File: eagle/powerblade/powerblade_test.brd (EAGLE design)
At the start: 123 x 88 mm, 78 parts, among them J1 JTAG_14PIN_IDC-NL, J21 AC_INFILM, Q1 2N7002, U1 TPS62122, U2 AD524, U3 MSP430FR5738, U4 LTC5800, U5 MAX9910, U6 MAX9910

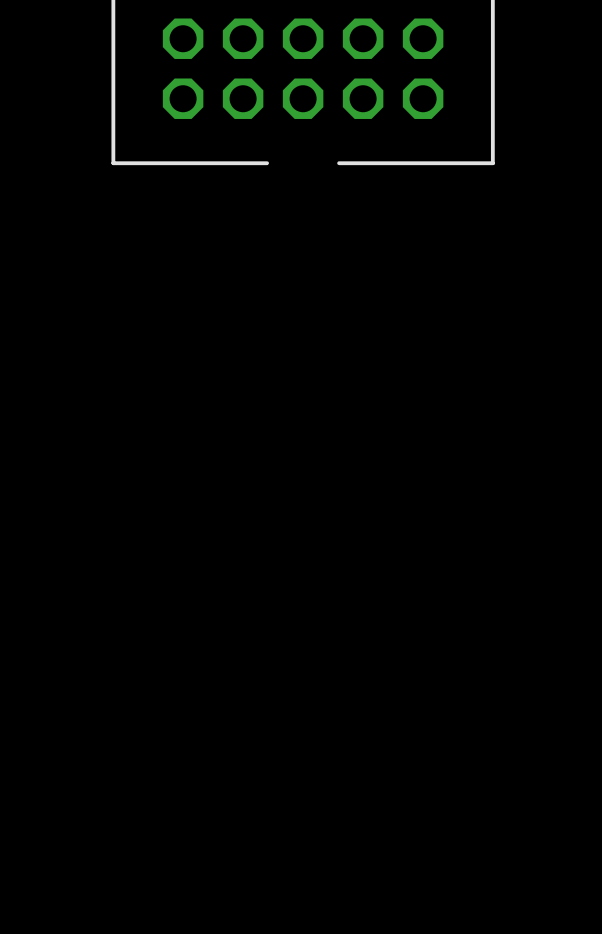
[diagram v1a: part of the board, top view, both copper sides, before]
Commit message: added crystals to ltc5800 sch in powerblade test
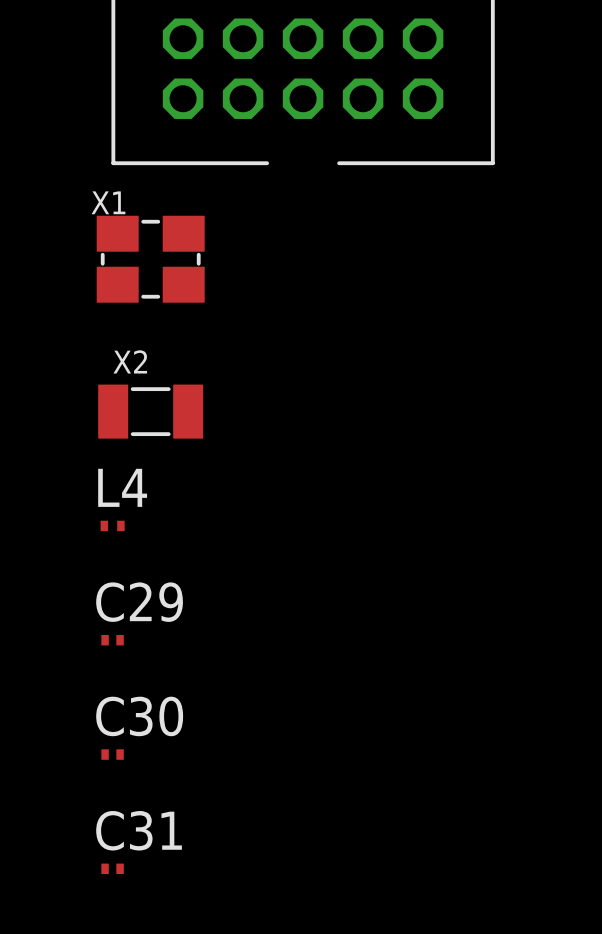
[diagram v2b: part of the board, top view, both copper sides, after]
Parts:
- added C29, C30: 1pF, rcl:C0201
- added C31: 100pF, rcl:C0201
- added L4: 3.3nH, rcl:L0201
- added X1: ABM8G, powerfilm:ABM8G
- added X2: ABS07, powerfilm:ABS07
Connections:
- new net N$42: U4.P29, X1.P1
- new net N$43: U4.P28, X1.P3
- new net N$44: U4.P20, X2.P2
- new net N$45: U4.P19, X2.P1
- new net N$46: C29.1, L4.2, U4.P14
- new net N$47: C30.1, C31.1, L4.1
- net GND: now also C29.2, C30.2, X1.P2, X1.P4
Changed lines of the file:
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@@
 <?xml version="1.0" encoding="utf-8"?>
 <!DOCTYPE eagle SYSTEM "eagle.dtd">
-<eagle version="6.3">
+<eagle version="6.5.0">
 <drawing>
 <settings>
@@
 <attribute name="DIGIKEY" value="WM18560-ND" x="-35.56" y="-135.89" size="1.778" layer="27" display="off"/>
 </element>
+<element name="X1" library="powerfilm" package="ABM8G" value="ABM8G" x="-40.64" y="-142.24">
+<attribute name="DIGIKEY" value="535-10293-1-ND" x="-40.64" y="-142.24" size="1.778" layer="27" display="off"/>
+</element>
+<element name="X2" library="powerfilm" package="ABS07" value="ABS07" x="-40.64" y="-147.32">
+<attribute name="DIGIKEY" value="535-12058-1-ND" x="-40.64" y="-147.32" size="1.778" layer="27" display="off"/>
+</element>
+<element name="L4" library="rcl" package="L0201" value="3.3nH" x="-41.91" y="-151.13"/>
+<element name="C29" library="rcl" package="C0201" value="1pF" x="-41.91" y="-154.94"/>
+<element name="C30" library="rcl" package="C0201" value="1pF" x="-41.91" y="-158.75"/>
+<element name="C31" library="rcl" package="C0201" value="100pF" x="-41.91" y="-162.56"/>
 </elements>
 <signals>
@@
 <vertex x="0" y="88.9"/>
 </polygon>
+<contactref element="X1" pad="P2"/>
+<contactref element="X1" pad="P4"/>
+<contactref element="C30" pad="2"/>
+<contactref element="C29" pad="2"/>
+<wire x1="-41.66" y1="-154.94" x2="-41.66" y2="-158.75" width="0" layer="19" extent="1-1"/>
+<wire x1="-39.54" y1="-143.09" x2="-41.66" y2="-154.94" width="0" layer="19" extent="1-1"/>
+<wire x1="-41.74" y1="-141.39" x2="-39.54" y2="-143.09" width="0" layer="19" extent="1-1"/>
+<wire x1="-33.56" y1="-134.89" x2="-39.54" y2="-143.09" width="0" layer="19" extent="1-1"/>
 <wire x1="-33.97" y1="-128.27" x2="-33.56" y2="-134.89" width="0" layer="19" extent="1-1"/>
 <wire x1="-37.78" y1="-128.27" x2="-33.97" y2="-128.27" width="0" layer="19" extent="1-1"/>
@@
 <wire x1="-38.1" y1="-25.4" x2="-41.26" y2="-66.04" width="0" layer="19" extent="1-1"/>
 <wire x1="-29.36875" y1="-23.23375" x2="-38.1" y2="-25.4" width="0" layer="19" extent="1-1"/>
+<wire x1="-27.375" y1="-23.61" x2="-29.36875" y2="-23.23375" width="0" layer="19" extent="1-1"/>
+<wire x1="-26.15" y1="-22.86" x2="-26.15" y2="-23.61" width="0" layer="19" extent="1-1"/>
+<wire x1="-25.4" y1="-22.86" x2="-25.4" y2="-23.61" width="0" layer="19" extent="1-1"/>
+<wire x1="-24.65" y1="-23.61" x2="-25.4" y2="-23.61" width="0" layer="19" extent="1-1"/>
+<wire x1="-26.15" y1="-22.11" x2="-26.15" y2="-22.86" width="0" layer="19" extent="1-1"/>
+<wire x1="-29.298" y1="-20.16125" x2="-27.375" y2="-21.61" width="0" layer="19" extent="1-1"/>
+<wire x1="-29.04" y1="-18.105" x2="-29.845" y2="-18.7325" width="0" layer="19" extent="1-1"/>
+<wire x1="-27.94" y1="-18.25625" x2="-29.04" y2="-18.105" width="0" layer="19" extent="1-1"/>
+<wire x1="-26.84" y1="-18.105" x2="-27.94" y2="-18.25625" width="0" layer="19" extent="1-1"/>
+<wire x1="-28.575" y1="-26.40875" x2="-27.375" y2="-23.61" width="0" layer="19" extent="1-1"/>
+<wire x1="-26.67" y1="-27.94" x2="-28.575" y2="-26.40875" width="0" layer="19" extent="1-1"/>
+<wire x1="-28.73375" y1="-13.59625" x2="-29.04" y2="-18.105" width="0" layer="19" extent="1-1"/>
+<wire x1="-27.305" y1="-13.59625" x2="-28.73375" y2="-13.59625" width="0" layer="19" extent="1-1"/>
+<wire x1="-27.305" y1="-12.3825" x2="-27.305" y2="-13.59625" width="0" layer="19" extent="1-1"/>
+<wire x1="-20.8788" y1="-14.76375" x2="-27.305" y2="-13.59625" width="0" layer="19" extent="1-1"/>
+<wire x1="-19.79625" y1="-13.9225" x2="-20.8788" y2="-14.76375" width="0" layer="19" extent="1-1"/>
+<wire x1="-17.78" y1="-18.25625" x2="-20.8788" y2="-14.76375" width="0" layer="19" extent="1-1"/>
+<wire x1="-18.25625" y1="-9.04875" x2="-19.79625" y2="-13.9225" width="0" layer="19" extent="1-1"/>
+<wire x1="-15.01625" y1="-9.271" x2="-18.25625" y2="-9.04875" width="0" layer="19" extent="1-1"/>
+<wire x1="-14.0462" y1="-9.486" x2="-15.01625" y2="-9.271" width="0" layer="19" extent="1-1"/>
+<wire x1="-12.85875" y1="-8.5748" x2="-14.0462" y2="-9.486" width="0" layer="19" extent="1-1"/>
+<wire x1="-11.58875" y1="-8.5748" x2="-12.85875" y2="-8.5748" width="0" layer="19" extent="1-1"/>
+<wire x1="-11.34975" y1="-8.80975" x2="-11.58875" y2="-8.5748" width="0" layer="19" extent="1-1"/>
+<wire x1="-6.8375" y1="-10.2085" x2="-9.38125" y2="-8.80975" width="0" layer="19" extent="1-1"/>
+<wire x1="-8.31125" y1="-12.7635" x2="-6.8375" y2="-10.2085" width="0" layer="19" extent="1-1"/>
+<wire x1="-11.43" y1="-20.955" x2="-17.78" y2="-18.25625" width="0" layer="19" extent="1-1"/>
 <wire x1="28.79" y1="6.35" x2="-6.8375" y2="-10.2085" width="0" layer="19" extent="1-1"/>
 </signal>
@@
 <contactref element="RI1" pad="1"/>
 </signal>
+<signal name="N$42">
+<contactref element="U4" pad="P29"/>
+<contactref element="X1" pad="P1"/>
+<wire x1="-37.35" y1="-30.25" x2="-41.74" y2="-143.09" width="0" layer="19" extent="1-1"/>
+</signal>
+<signal name="N$43">
+<contactref element="U4" pad="P28"/>
+<contactref element="X1" pad="P3"/>
+<wire x1="-37.85" y1="-30.25" x2="-39.54" y2="-141.39" width="0" layer="19" extent="1-1"/>
+</signal>
+<signal name="N$44">
+<contactref element="U4" pad="P20"/>
+<contactref element="X2" pad="P2"/>
+<wire x1="-41.85" y1="-30.25" x2="-39.39" y2="-147.32" width="0" layer="19" extent="1-1"/>
+</signal>
+<signal name="N$45">
+<contactref element="U4" pad="P19"/>
+<contactref element="X2" pad="P1"/>
+<wire x1="-42.35" y1="-30.25" x2="-41.89" y2="-147.32" width="0" layer="19" extent="1-1"/>
+</signal>
+<signal name="N$46">
+<contactref element="U4" pad="P14"/>
+<contactref element="L4" pad="2"/>
+<contactref element="C29" pad="1"/>
+<wire x1="-41.635" y1="-151.13" x2="-42.16" y2="-154.94" width="0" layer="19" extent="1-1"/>
+<wire x1="-42.95" y1="-27.65" x2="-41.635" y2="-151.13" width="0" layer="19" extent="1-1"/>
+</signal>
+<signal name="N$47">
+<contactref element="L4" pad="1"/>
+<contactref element="C31" pad="1"/>
+<contactref element="C30" pad="1"/>
+<wire x1="-42.16" y1="-158.75" x2="-42.16" y2="-162.56" width="0" layer="19" extent="1-1"/>
+<wire x1="-42.185" y1="-151.13" x2="-42.16" y2="-158.75" width="0" layer="19" extent="1-1"/>
+</signal>
 </signals>

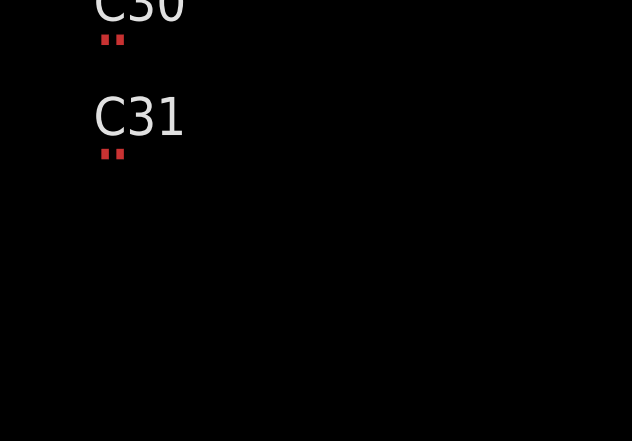
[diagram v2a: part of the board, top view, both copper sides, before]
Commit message: added antenna and programming header to ltc5800 schematic
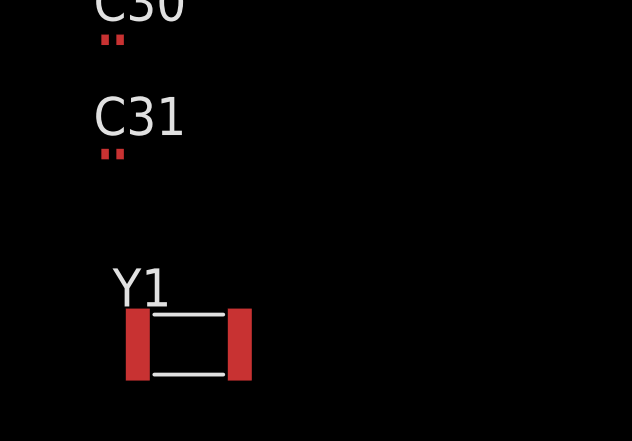
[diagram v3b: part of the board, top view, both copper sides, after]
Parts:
- added Y1: UREACH_XTEND, powerfilm:UREACH_XTEND
- C29: value 1pF -> 1.2pF
- C30: value 1pF -> NP
- C31: value 100pF -> 0ohm
- L4: value 3.3nH -> 7.5nH
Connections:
- new net FLASH_EN: SV1.2, U4.P55
- new net IPC_MISO: SV1.5, U4.P40
- new net IPC_MOSI: SV1.4, U4.P42
- new net IPC_SCK: SV1.3, U4.P44
- new net IPC_SS: SV1.1, U4.P45
- new net N$48: C31.2, Y1.P1
- new net UC_RX: SV1.10, U4.P38
- new net UC_TX: SV1.9, U4.P37
- net +3V3: now also SV1.7
- net NRST: now also SV1.6
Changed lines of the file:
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@@
 <?xml version="1.0" encoding="utf-8"?>
 <!DOCTYPE eagle SYSTEM "eagle.dtd">
-<eagle version="6.5.0">
+<eagle version="6.3">
 <drawing>
 <settings>
@@
 <attribute name="DIGIKEY" value="535-12058-1-ND" x="-40.64" y="-147.32" size="1.778" layer="27" display="off"/>
 </element>
-<element name="L4" library="rcl" package="L0201" value="3.3nH" x="-41.91" y="-151.13"/>
-<element name="C29" library="rcl" package="C0201" value="1pF" x="-41.91" y="-154.94"/>
-<element name="C30" library="rcl" package="C0201" value="1pF" x="-41.91" y="-158.75"/>
-<element name="C31" library="rcl" package="C0201" value="100pF" x="-41.91" y="-162.56"/>
+<element name="L4" library="rcl" package="L0201" value="7.5nH" x="-41.91" y="-151.13"/>
+<element name="C29" library="rcl" package="C0201" value="1.2pF" x="-41.91" y="-154.94"/>
+<element name="C30" library="rcl" package="C0201" value="NP" x="-41.91" y="-158.75"/>
+<element name="C31" library="rcl" package="C0201" value="0ohm" x="-41.91" y="-162.56"/>
+<element name="Y1" library="powerfilm" package="UREACH_XTEND" value="UREACH_XTEND" x="-39.37" y="-168.91">
+<attribute name="FRACTUS" value="FR05-S1-N-0-110" x="-39.37" y="-168.91" size="1.778" layer="27" display="off"/>
+</element>
 </elements>
 <signals>
@@
 <contactref element="R15" pad="1"/>
 <contactref element="L2" pad="1"/>
+<contactref element="SV1" pad="7"/>
+<wire x1="-32.07" y1="-127.62" x2="-33.56" y2="-136.89" width="0" layer="19" extent="1-1"/>
+<wire x1="-35.88" y1="-127.62" x2="-32.07" y2="-127.62" width="0" layer="19" extent="1-1"/>
+<wire x1="-36.21" y1="-123.19" x2="-35.88" y2="-127.62" width="0" layer="19" extent="1-1"/>
+<wire x1="-42.56" y1="-123.19" x2="-36.21" y2="-123.19" width="0" layer="19" extent="1-1"/>
 <wire x1="-41.06" y1="-118.11" x2="-42.56" y2="-123.19" width="0" layer="19" extent="1-1"/>
-<wire x1="-36.21" y1="-123.19" x2="-42.56" y2="-123.19" width="0" layer="19" extent="1-1"/>
-<wire x1="-35.88" y1="-127.62" x2="-36.21" y2="-123.19" width="0" layer="19" extent="1-1"/>
-<wire x1="-32.07" y1="-127.62" x2="-35.88" y2="-127.62" width="0" layer="19" extent="1-1"/>
 <wire x1="-31.33" y1="-102.87" x2="-41.06" y2="-118.11" width="0" layer="19" extent="1-1"/>
 <wire x1="-42.76" y1="-97.79" x2="-31.33" y2="-102.87" width="0" layer="19" extent="1-1"/>
 <wire x1="-22.70125" y1="-29.21" x2="-42.76" y2="-97.79" width="0" layer="19" extent="1-1"/>
+<wire x1="-29.04" y1="-17.455" x2="-29.04" y2="-16.805" width="0" layer="19" extent="1-1"/>
+<wire x1="-28.73375" y1="-15.29625" x2="-29.04" y2="-16.805" width="0" layer="19" extent="1-1"/>
 </signal>
 <signal name="RST">
@@
 <signal name="NRST">
 <contactref element="U4" pad="P22"/>
+<contactref element="SV1" pad="6"/>
+<wire x1="-40.85" y1="-30.25" x2="-35.56" y2="-134.89" width="0" layer="19" extent="1-1"/>
 </signal>
 <signal name="N$37">
@@
 <wire x1="-42.185" y1="-151.13" x2="-42.16" y2="-158.75" width="0" layer="19" extent="1-1"/>
 </signal>
+<signal name="N$48">
+<contactref element="C31" pad="2"/>
+<contactref element="Y1" pad="P1"/>
+<wire x1="-41.66" y1="-162.56" x2="-41.07" y2="-168.91" width="0" layer="19" extent="1-1"/>
+</signal>
+<signal name="IPC_SS">
+<contactref element="SV1" pad="1"/>
+<contactref element="U4" pad="P45"/>
+<wire x1="-33.25" y1="-25.65" x2="-39.56" y2="-136.89" width="0" layer="19" extent="1-1"/>
+</signal>
+<signal name="IPC_SCK">
+<contactref element="SV1" pad="3"/>
+<contactref element="U4" pad="P44"/>
+<wire x1="-33.25" y1="-26.15" x2="-37.56" y2="-136.89" width="0" layer="19" extent="1-1"/>
+</signal>
+<signal name="IPC_MISO">
+<contactref element="SV1" pad="5"/>
+<contactref element="U4" pad="P40"/>
+<wire x1="-33.25" y1="-28.15" x2="-35.56" y2="-136.89" width="0" layer="19" extent="1-1"/>
+</signal>
+<signal name="UC_TX">
+<contactref element="SV1" pad="9"/>
+<contactref element="U4" pad="P37"/>
+<wire x1="-33.25" y1="-29.65" x2="-31.56" y2="-136.89" width="0" layer="19" extent="1-1"/>
+</signal>
+<signal name="FLASH_EN">
+<contactref element="SV1" pad="2"/>
+<contactref element="U4" pad="P55"/>
+<wire x1="-33.85" y1="-20.55" x2="-39.56" y2="-134.89" width="0" layer="19" extent="1-1"/>
+</signal>
+<signal name="IPC_MOSI">
+<contactref element="SV1" pad="4"/>
+<contactref element="U4" pad="P42"/>
+<wire x1="-33.25" y1="-27.15" x2="-37.56" y2="-134.89" width="0" layer="19" extent="1-1"/>
+</signal>
+<signal name="UC_RX">
+<contactref element="SV1" pad="10"/>
+<contactref element="U4" pad="P38"/>
+<wire x1="-33.25" y1="-29.15" x2="-31.56" y2="-134.89" width="0" layer="19" extent="1-1"/>
+</signal>
 </signals>

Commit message: added tr1000 to powerblade test sch
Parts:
- added C32, C33, C34: NP, rcl:C0603
- added C35: 27pF, rcl:C0603
- added C36: 100pF, rcl:C0603
- added C37: 4.7uF, rcl:CPOL-0805
- added R22: 270k, rcl:R0603
- added R23, R24, R27: 0, rcl:R0603
- added R25, R33, R34: NP, rcl:R0603
- added R26, R29: 100k, rcl:R0603
- added R28: 330k, rcl:R0603
- added R30: 4.7k, rcl:R0603
- added R31, R32: 4.99k, rcl:R0603
- C2: value 0.1uF -> 15nF
- R12: value 660 -> NP
- U2: value AD524 -> TR1000; device powerfilm:SOT-23-8 -> powerfilm:SM-20H
- moved R12 243.2 mm to (-50.8, -256.5), turned to 0 degrees
- moved C2 197.6 mm to (-50.8, -210.8), turned to 0 degrees
- moved U2 147.5 mm to (-48.3, -163.8)
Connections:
- removed net SCL: U2.P4, U3.P17
- removed net SDA: U2.P5, U3.P16
- new net CNT0: R32.2, U2.P18, U3.P1
- new net CNT1: R31.2, U2.P17, U3.P2
- new net N$49: C34.1, R23.1, U2.P3
- new net N$50: R12.2, R22.2, U2.P15
- new net N$51: R28.2, U2.P14
- new net N$52: R29.2, U2.P9
- new net N$53: R30.2, U2.P8
- new net N$54: C2.2, C32.1, R27.2
- new net N$55: C2.1, U2.P6
- new net N$56: R24.2, R25.2, R26.1, U2.P11
- new net N$57: R24.1, U2.P13
- new net N$58: R25.1, U2.P12
- new net N$59: C33.1, U2.P4
- new net N$60: R33.1, U3.P13
- new net N$61: R34.1, U3.P14
- new net RXDATA: R34.2, U2.P7, U3.P4
- new net TXMOD: R30.1, R33.2, U3.P3
- net +3V3: now also C35.1, C36.1, C37.+, R12.1, R23.2, U2.P16; no longer C2.1, U2.P1
- net GND: now also C32.2, C33.2, C34.2, C35.2, C36.2, C37.-, R22.1, R26.2, R28.1, R29.1, R31.1, R32.1, U2.P1, U2.P10, U2.P19; no longer C2.2, R12.1, U2.P3, U2.P6
- net N$12: now also R27.1, U2.P5; no longer R12.2, U2.P7
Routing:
- net SCL: track 4.63 -> 0.00 mm
- net N$12: track 3.81 -> 0.00 mm
- net SDA: track 2.92 -> 0.00 mm
- net +3V3: track 51.5 -> 50.5 mm

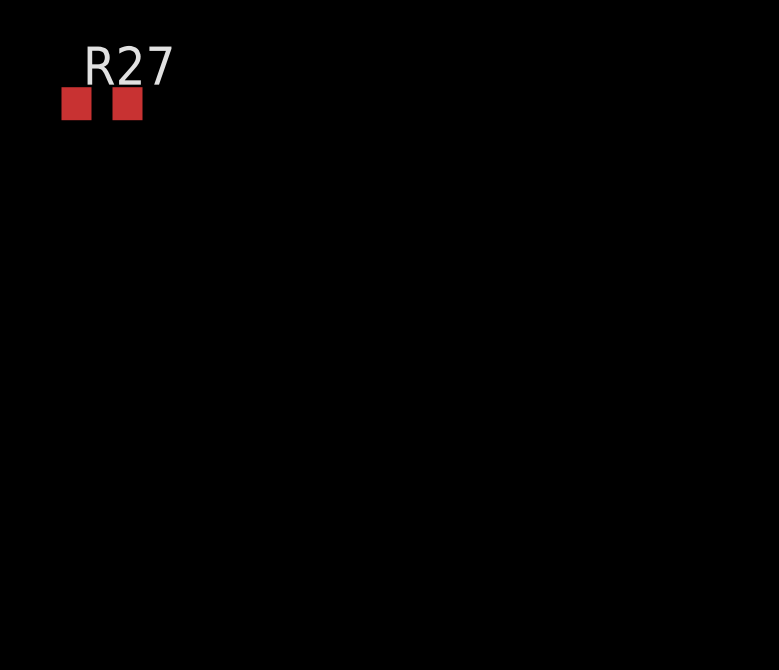
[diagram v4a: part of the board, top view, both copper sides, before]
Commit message: added antenna to tr1000 circuit
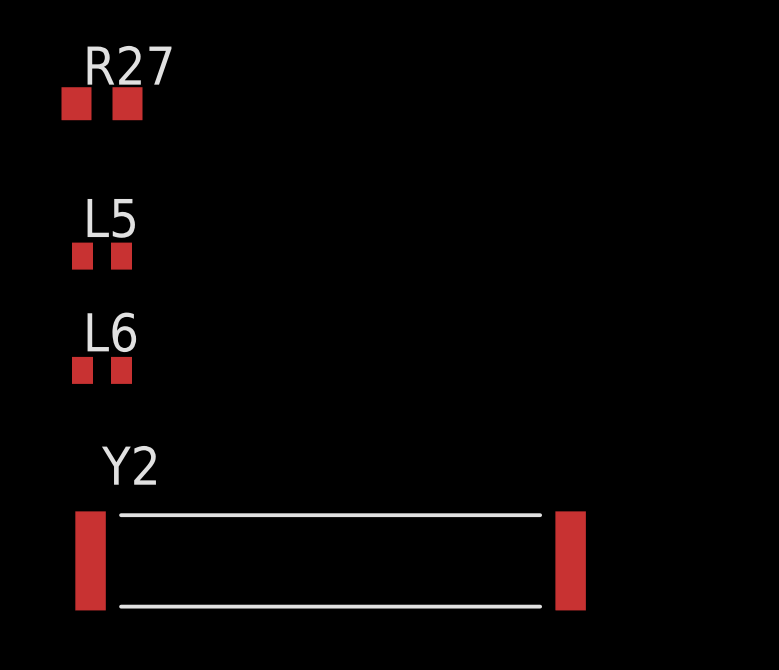
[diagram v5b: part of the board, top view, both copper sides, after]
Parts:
- added L5: 10nH, rcl:L0402
- added L6: 100nH, rcl:L0402
- added Y2: ANT-916, powerfilm:ANT-916
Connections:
- new net N$62: L5.2, U2.P20
- new net N$63: L5.1, L6.1, Y2.P1
- net GND: now also L6.2
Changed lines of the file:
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@@
 <element name="R26" library="rcl" package="R0603" value="100k" x="-50.8" y="-302.26"/>
 <element name="R27" library="rcl" package="R0603" value="0" x="-50.8" y="-307.34"/>
+<element name="L5" library="rcl" package="L0402" value="10nH" x="-50.8" y="-312.42"/>
+<element name="L6" library="rcl" package="L0402" value="100nH" x="-50.8" y="-316.23"/>
+<element name="Y2" library="powerfilm" package="ANT-916" value="ANT-916" x="-43.18" y="-322.58">
+<attribute name="DIGIKEY" value="ANT-916-CHP-TCT-ND" x="-43.18" y="-322.58" size="1.778" layer="27" display="off"/>
+</element>
 </elements>
 <signals>
@@
 <contactref element="R32" pad="1"/>
 <contactref element="R26" pad="2"/>
+<contactref element="L6" pad="2"/>
 <wire x1="-45.466" y1="-160.274" x2="-48.768" y2="-168.2115" width="0" layer="19" extent="1-1"/>
 <wire x1="-48.768" y1="-159.4485" x2="-45.466" y2="-160.274" width="0" layer="19" extent="1-1"/>
@@
 <wire x1="-51.65" y1="-287.02" x2="-51.65" y2="-281.94" width="0" layer="19" extent="1-1"/>
 <wire x1="-49.95" y1="-302.26" x2="-51.65" y2="-287.02" width="0" layer="19" extent="1-1"/>
+<wire x1="-50.15" y1="-316.23" x2="-49.95" y2="-302.26" width="0" layer="19" extent="1-1"/>
 </signal>
 <signal name="VCC">
@@
 <wire x1="-24.65" y1="-20.885" x2="-51.65" y2="-251.46" width="0" layer="19" extent="1-1"/>
 </signal>
+<signal name="N$62">
+<contactref element="U2" pad="P20"/>
+<contactref element="L5" pad="2"/>
+<wire x1="-50.15" y1="-312.42" x2="-47.752" y2="-159.4485" width="0" layer="19" extent="1-1"/>
+</signal>
+<signal name="N$63">
+<contactref element="L5" pad="1"/>
+<contactref element="Y2" pad="P1"/>
+<contactref element="L6" pad="1"/>
+<wire x1="-51.45" y1="-316.23" x2="-51.181" y2="-322.58" width="0" layer="19" extent="1-1"/>
+<wire x1="-51.45" y1="-312.42" x2="-51.45" y2="-316.23" width="0" layer="19" extent="1-1"/>
+</signal>
 </signals>
